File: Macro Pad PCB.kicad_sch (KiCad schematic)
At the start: 25 parts, among them U1 RP2040, Y1 12MHz

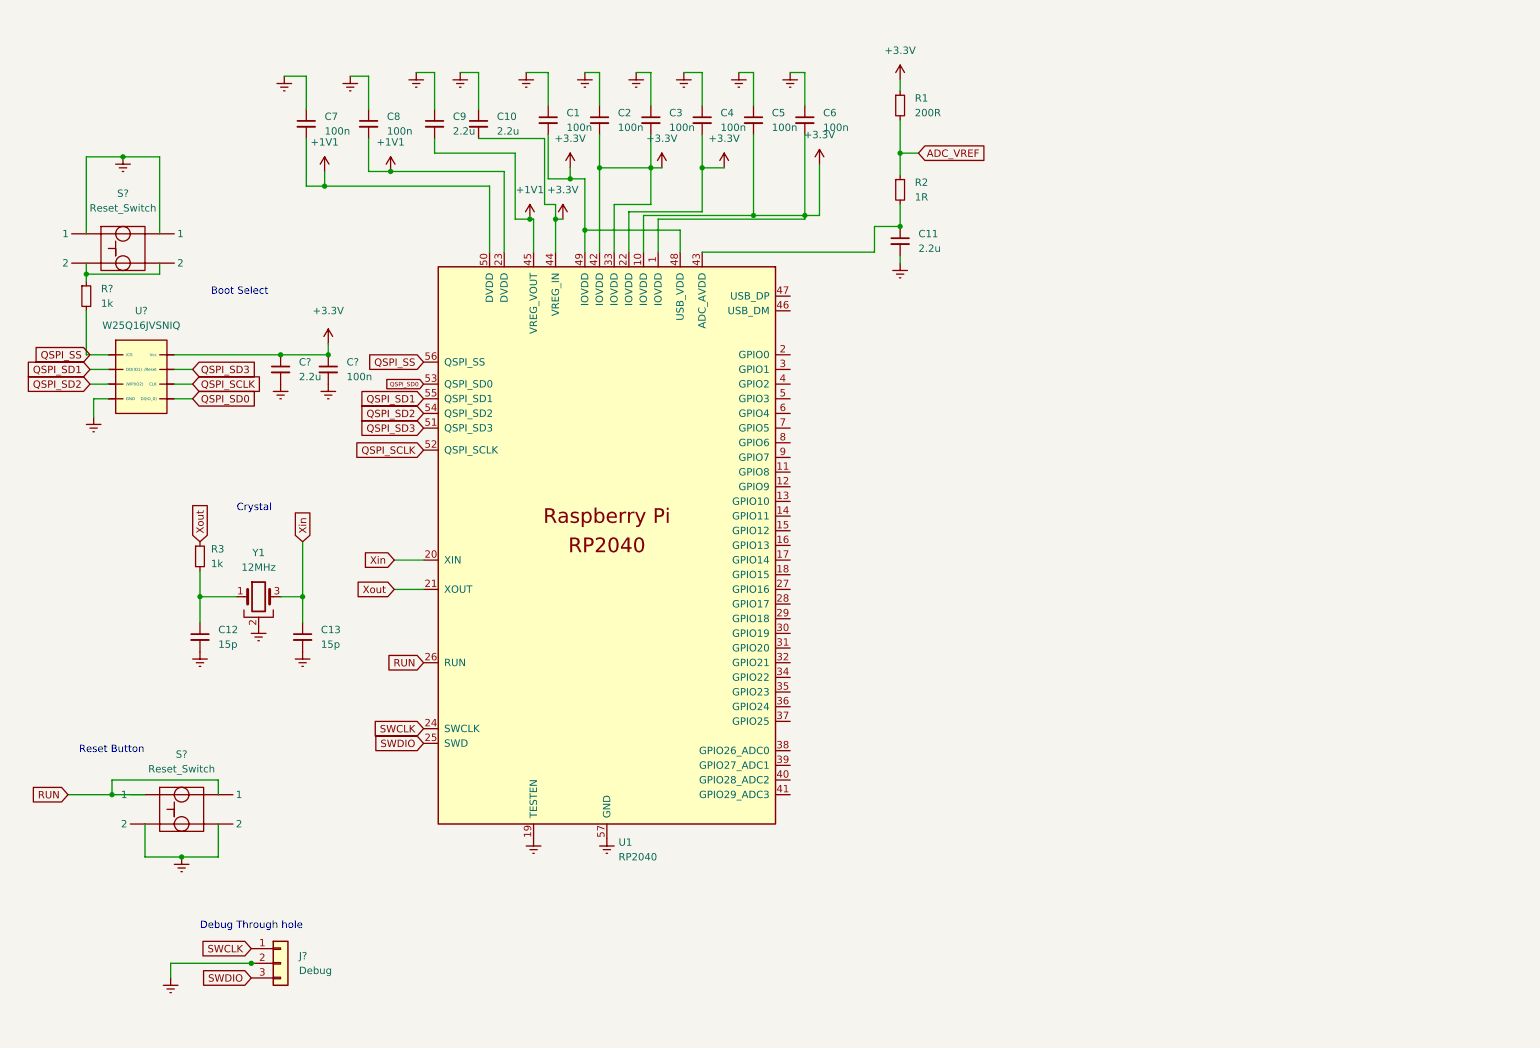
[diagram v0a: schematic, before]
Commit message: Added DC-DC Converter
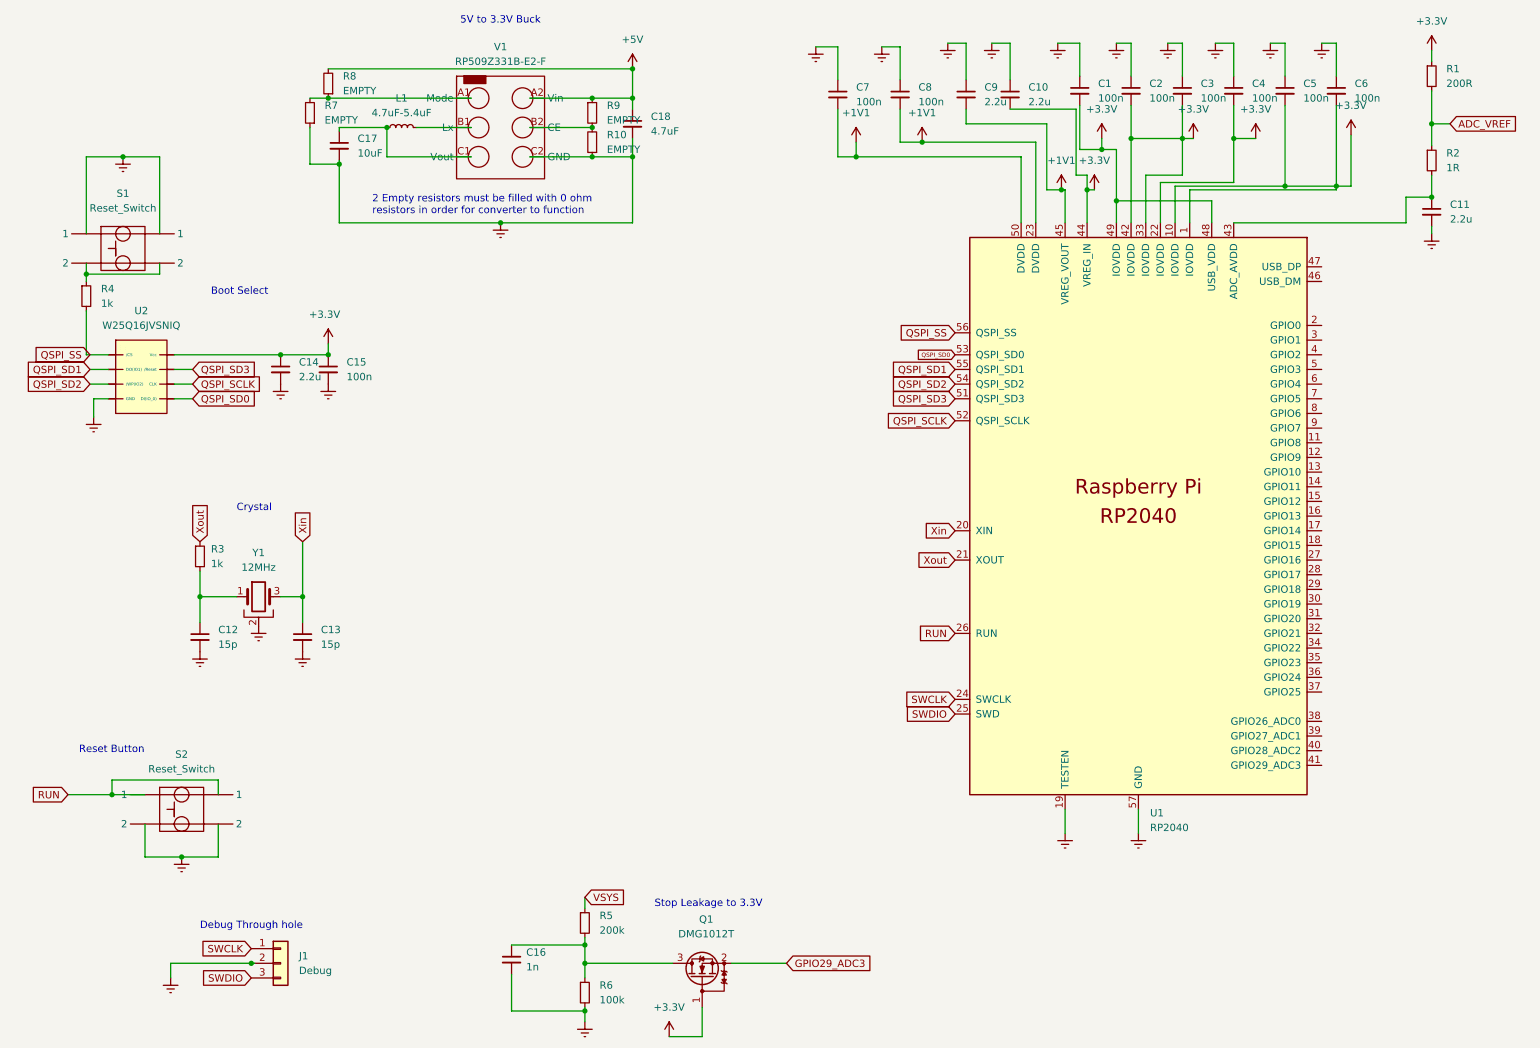
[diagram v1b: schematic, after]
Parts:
- added C16: 1n, symbol Device:C_Small
- added C17: 10uF, symbol Device:C_Small
- added C18: 4.7uF, symbol Device:C_Small
- added L1: 4.7uF-5.4uF, symbol Device:L_Small
- added Q1: DMG1012T, Package_TO_SOT_SMD:SOT-523, symbol Transistor_FET:DMG1012T
- added R10, R7, R8, R9: EMPTY, symbol Device:R_Small
- added R5: 200k, symbol Device:R_Small
- added R6: 100k, symbol Device:R_Small
- added V1: RP509Z331B-E2-F, symbol Reset Switch:RP509Z331B-E2-F
- C2, C3, C4, C6: footprint (none) -> Capacitor_SMD:C_0201_0603Metric_Pad0.64x0.40mm_HandSolder
- gave numbers to parts that had none: 7
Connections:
- net +3.3V: now also Q1.1 (G)
- net Earth: now also C16.2, C17.2, C18.2, R10.1, R6.2, R7.1, V1.C2 (GND)
- new net: R7.2, R8.1, V1.A1 (Mode)
- new net: R10.2, R9.2, V1.B2 (CE)
- new net: C16.1, Q1.3 (D), R5.2, R6.1
- new net: C17.1, L1.1, V1.C1 (Vout)
- new net: L1.2, V1.B1 (Lx)
- new net +5V: C18.1, R8.2, R9.1, V1.A2 (Vin)
- new net GPIO29_ADC3: Q1.2 (S)
- new net VSYS: R5.1
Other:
- note added: "2 Empty resistors must be filled with 0 ohm resistors in order for converter to function"
- note added: "5V to 3.3V Buck"
- note added: "Stop Leakage to 3.3V"
- moved on the sheet: C1, C10, C11, C2, C3, C4, C5, C6, C7, C8, C9, R1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

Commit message: Added Key Matrix
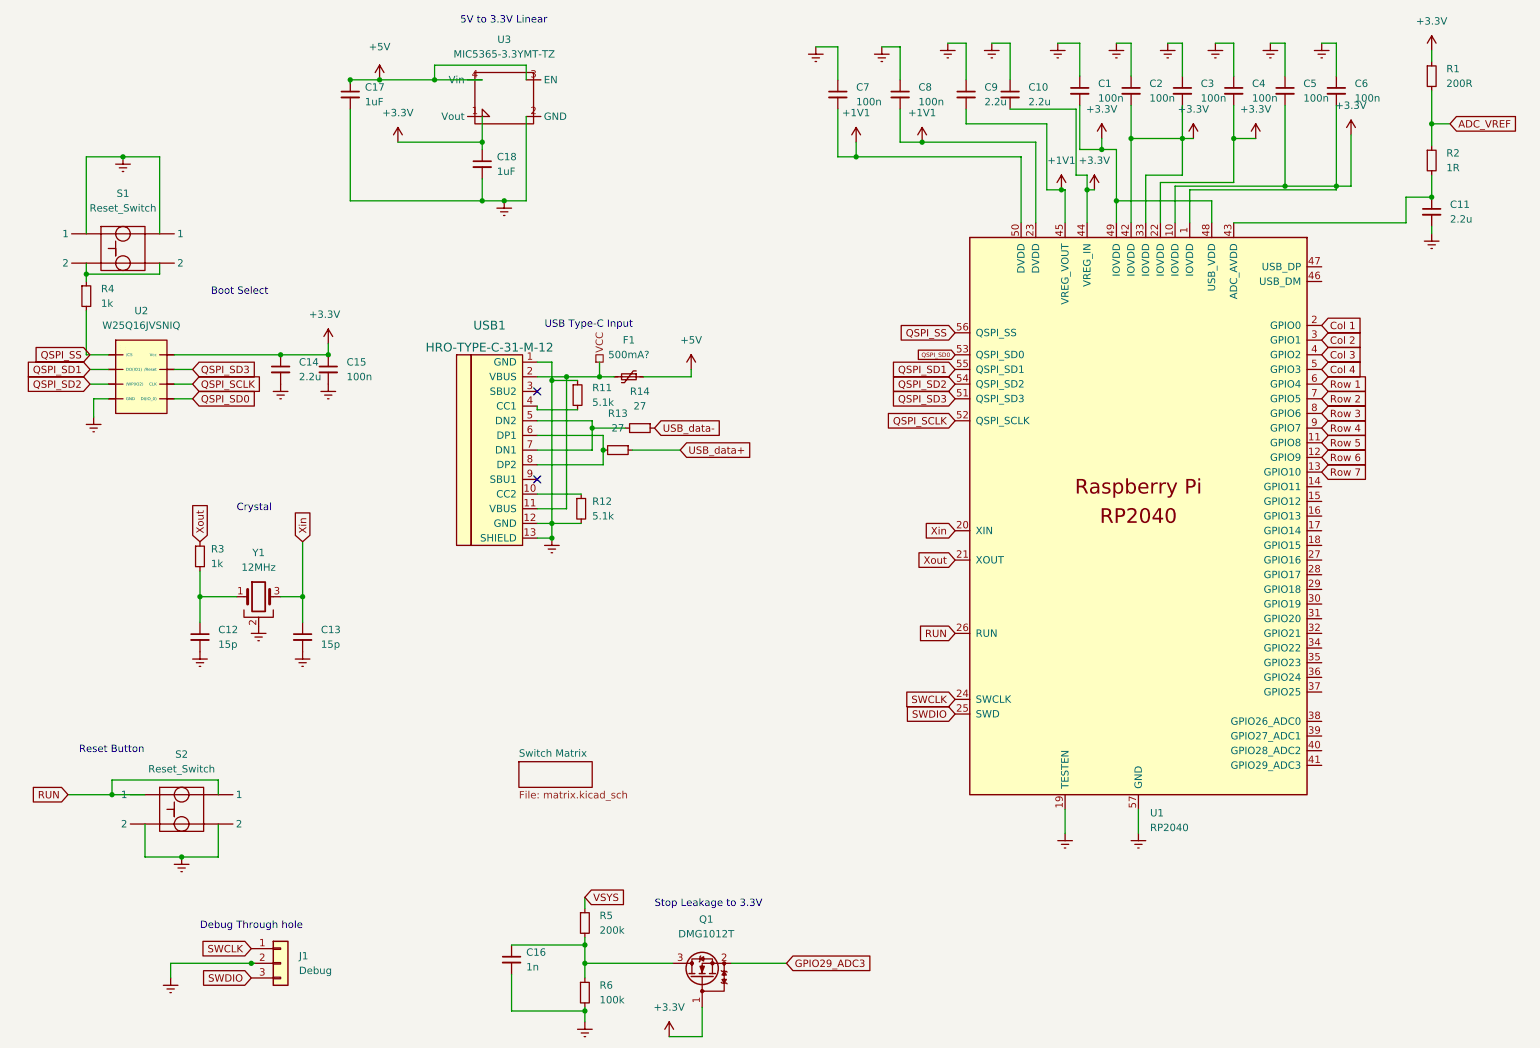
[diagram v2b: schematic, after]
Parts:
- removed L1: 4.7uF-5.4uF, symbol Device:L_Small
- removed R10, R7, R8, R9: EMPTY, symbol Device:R_Small
- removed V1: RP509Z331B-E2-F, symbol Reset Switch:RP509Z331B-E2-F
- added F1: 500mA?, symbol Device:Polyfuse_Small
- added R11, R12: 5.1k, symbol Device:R_Small
- added R13, R14: 27, symbol Device:R_Small
- added U3: MIC5365-3.3YMT-TZ, symbol Reset Switch:MIC5365-3.3YMT-TZ
- added USB1: HRO-TYPE-C-31-M-12, symbol Type-C:HRO-TYPE-C-31-M-12
- C17: value 10uF -> 1uF
- C18: value 4.7uF -> 1uF
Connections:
- net +3.3V: now also C18.1, U3.1 (Vout)
- net +5V: now also C17.1, F1.1, U3.3 (EN), U3.4 (Vin); no longer C18.1
- net Earth: now also R11.1, R12.2, U3.2 (GND), USB1.1 (GND), USB1.12 (GND), USB1.13 (SHIELD)
- net Row 5: now reaches U1.11 (GPIO8)
- net Row 6: now reaches U1.12 (GPIO9)
- net Row 7: now reaches U1.13 (GPIO10)
- net Col 1: now reaches U1.2 (GPIO0)
- net Col 2: now reaches U1.3 (GPIO1)
- net Col 3: now reaches U1.4 (GPIO2)
- net Col 4: now reaches U1.5 (GPIO3)
- net Row 1: now reaches U1.6 (GPIO4)
- net Row 2: now reaches U1.7 (GPIO5)
- net Row 3: now reaches U1.8 (GPIO6)
- net Row 4: now reaches U1.9 (GPIO7)
- new net: R13.2, USB1.6 (DP1), USB1.8 (DP2)
- new net: R12.1, USB1.10 (CC2)
- new net: R11.2, USB1.4 (CC1)
- new net: R14.2, USB1.5 (DN2), USB1.7 (DN1)
- new net USB_data+: R13.1
- new net USB_data-: R14.1
- new net VCC: F1.2, USB1.11 (VBUS), USB1.2 (VBUS)
- no-connect marks 0 -> 2
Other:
- added sheet Switch Matrix (matrix.kicad_sch)
- note added: "5V to 3.3V Linear"
- note added: "USB Type-C Input"
- note removed: "2 Empty resistors must be filled with 0 ohm resistors in order for converter to function"
- note removed: "5V to 3.3V Buck"
